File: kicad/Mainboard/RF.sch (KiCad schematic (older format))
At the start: 111 parts, among them J8 Antenna, Q3 BGA6589, Q7 FDV304P, T1 AFT05MS004NT1, U13 BGA2874, U5 ADF7021, U6 HMC546MS8GETR, U7 LM2904A, X1 12.288MHz

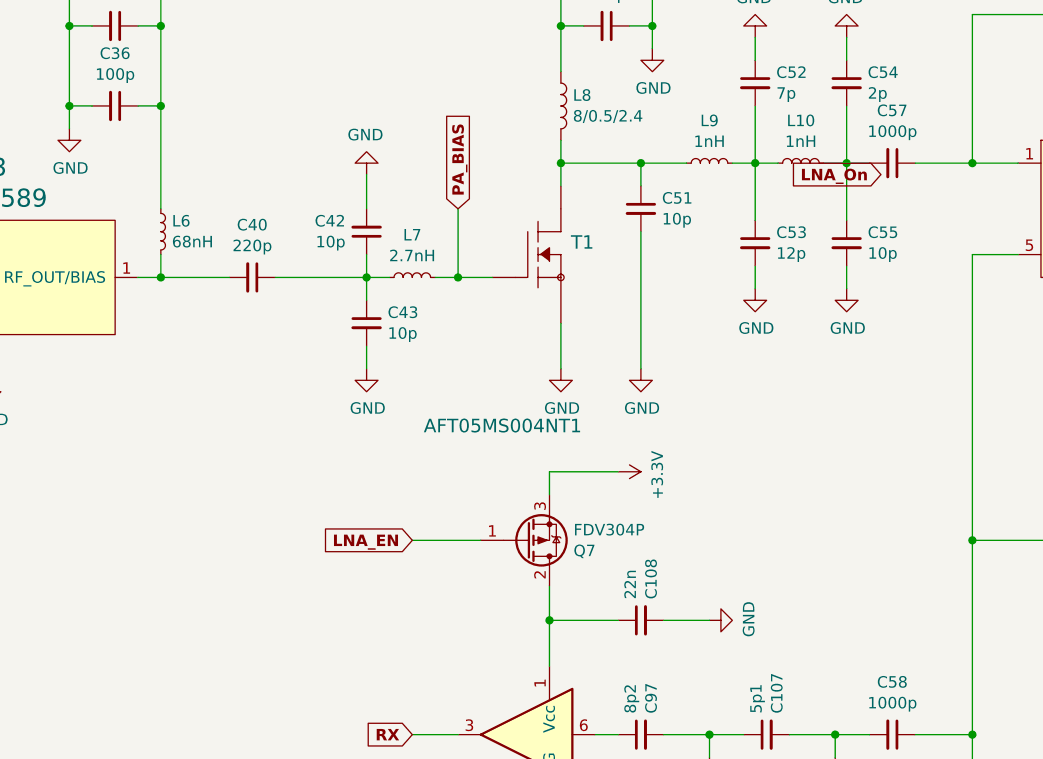
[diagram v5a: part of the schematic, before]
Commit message: Added some vias and forgotten power supply lines & plotted pdf schematic
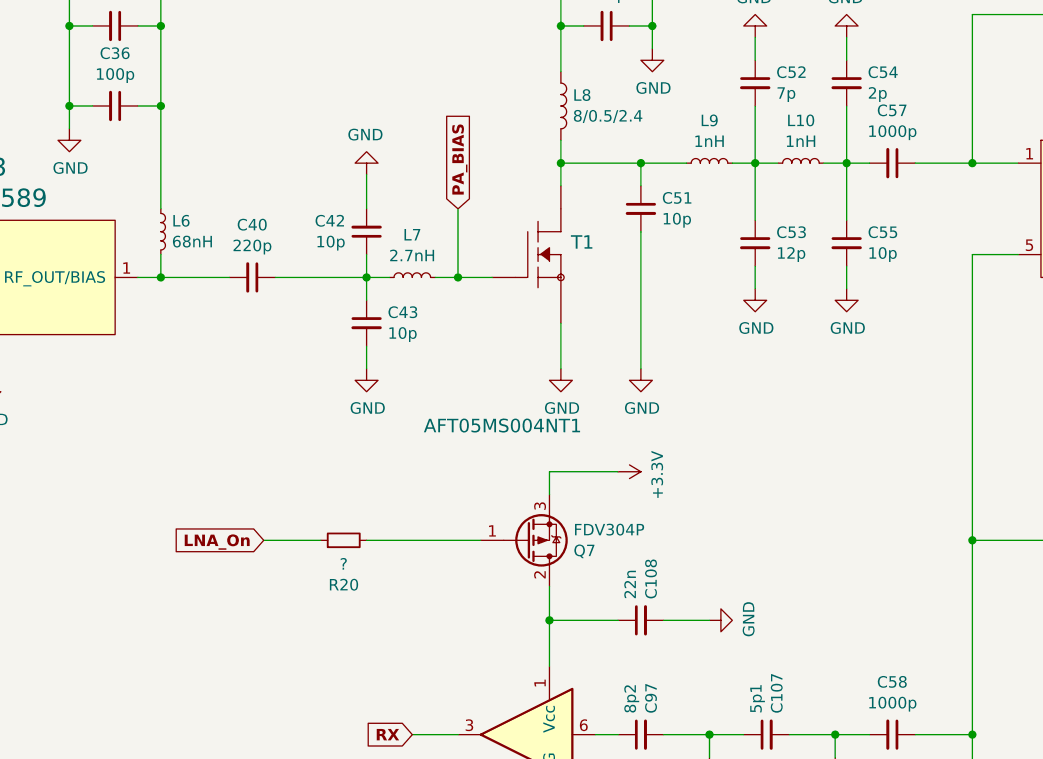
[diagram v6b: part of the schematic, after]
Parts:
- added R20: ?, Resistor_SMD:R_0603_1608Metric, symbol Mainboard-rescue:R_Small-Device
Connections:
- net LNA_On: now also R20.1
- net LNA_EN: no longer names the net of Q7.1 (G)
- net LNA_EN: now also R20.2
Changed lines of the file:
@@
 EESchema Schematic File Version 4
-LIBS:Mainboard-cache
 EELAYER 30 0
 EELAYER END
@@
 	1    0    0    1
 $EndComp
-Text GLabel 5700 4150 0    50   Input ~ 10
-LNA_EN
-Text GLabel 7750 2550 0    50   Input ~ 10
+Text GLabel 5050 4150 0    50   Input ~ 10
 LNA_On
-Wire Wire Line
-	5700 4150 6000 4150
 Wire Wire Line
 	6300 4500 6600 4500
@@
 Wire Wire Line
 	7900 5000 8150 5000
+$Comp
+L Mainboard-rescue:R_Small-Device R20
+U 1 1 5EE52FB1
+P 5400 4150
+F 0 "R20" V 5204 4150 50  0000 C CNN
+F 1 "?" V 5295 4150 50  0000 C CNN
+F 2 "Resistor_SMD:R_0603_1608Metric" H 5400 4150 50  0001 C CNN
+F 3 "~" H 5400 4150 50  0001 C CNN
+	1    5400 4150
+	0    -1   -1   0
+$EndComp
+Wire Wire Line
+	5500 4150 6000 4150
+Wire Wire Line
+	5300 4150 5050 4150
 $EndSCHEMATC

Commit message: added vias, and long soldering pads(for shielding) around RF Amplifier part, added more vias near STM32, added 3D visualizaton of PCB!
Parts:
- L8: footprint TR-9:RF_Coil -> TR-9:RF_Coil_v2_mirrored
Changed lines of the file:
@@
 F 0 "L8" H 6402 2296 50  0000 L CNN
 F 1 "8/0.5/2.4" H 6402 2205 50  0000 L CNN
-F 2 "TR-9:RF_Coil" H 6350 2250 50  0001 C CNN
+F 2 "TR-9:RF_Coil_v2_mirrored" H 6350 2250 50  0001 C CNN
 F 3 "~" H 6350 2250 50  0001 C CNN
 	1    6350 2250

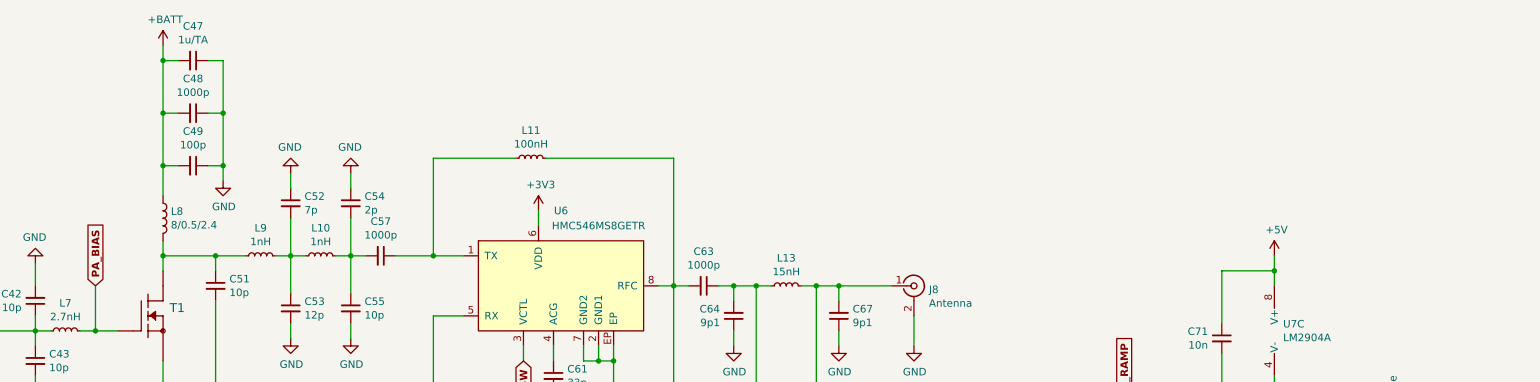
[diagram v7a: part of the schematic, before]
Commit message: added a JCx symbols - these are Jumper Cables - them are used to avoid EMI diseaster when trying to route Power signals under RF 50 ohm trace - also added them to PCB +  Schematic in PDF plotted; TODO - more signal integrity improvement
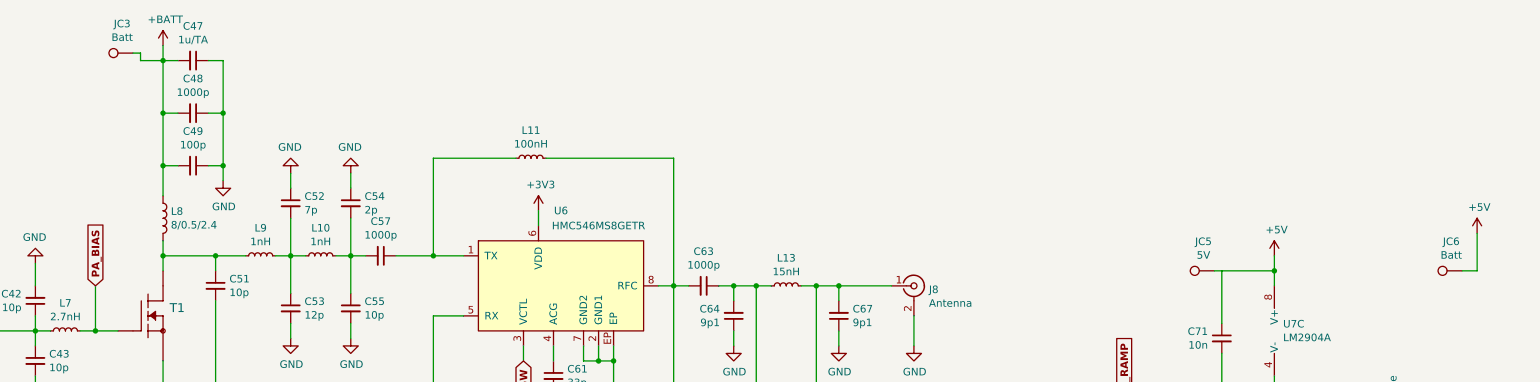
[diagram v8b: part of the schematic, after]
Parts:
- added JC3, JC6: Batt, TR-9:Pad1x3, symbol Connector:TestPoint
- added JC5: 5V, TR-9:Pad1x3, symbol Connector:TestPoint
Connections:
- net +5V: now also JC5.1, JC6.1
- net +BATT: now also JC3.1
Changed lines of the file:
@@
 Wire Wire Line
 	5300 4150 5050 4150
+$Comp
+L Connector:TestPoint JC?
+U 1 1 5F012C9B
+P 6150 1150
+AR Path="/5DFC2ACA/5F012C9B" Ref="JC?"  Part="1"
+AR Path="/5DF0E505/5F012C9B" Ref="JC3"  Part="1"
+F 0 "JC3" V 6345 1222 50  0000 C CNN
+F 1 "Batt" V 6254 1222 50  0000 C CNN
+F 2 "TR-9:Pad1x3" H 6350 1150 50  0001 C CNN
+F 3 "~" H 6350 1150 50  0001 C CNN
+	1    6150 1150
+	0    -1   -1   0
+$EndComp
+Wire Wire Line
+	6150 1150 6200 1150
+Wire Wire Line
+	6200 1150 6200 1200
+Wire Wire Line
+	6200 1200 6350 1200
+$Comp
+L Connector:TestPoint JC?
+U 1 1 5F0B8C39
+P 13350 2600
+AR Path="/5DFC2ACA/5F0B8C39" Ref="JC?"  Part="1"
+AR Path="/5DF0E505/5F0B8C39" Ref="JC5"  Part="1"
+F 0 "JC5" V 13545 2672 50  0000 C CNN
+F 1 "5V" V 13454 2672 50  0000 C CNN
+F 2 "TR-9:Pad1x3" H 13550 2600 50  0001 C CNN
+F 3 "~" H 13550 2600 50  0001 C CNN
+	1    13350 2600
+	0    -1   -1   0
+$EndComp
+Wire Wire Line
+	13350 2600 13400 2600
+$Comp
+L power:+5V #PWR0213
+U 1 1 5F0D81B0
+P 15100 2350
+F 0 "#PWR0213" H 15100 2200 50  0001 C CNN
+F 1 "+5V" H 15115 2523 50  0000 C CNN
+F 2 "" H 15100 2350 50  0001 C CNN
+F 3 "" H 15100 2350 50  0001 C CNN
+	1    15100 2350
+	1    0    0    -1
+$EndComp
+$Comp
+L Connector:TestPoint JC?
+U 1 1 5F0D8B7F
+P 15000 2600
+AR Path="/5DFC2ACA/5F0D8B7F" Ref="JC?"  Part="1"
+AR Path="/5DF0E505/5F0D8B7F" Ref="JC6"  Part="1"
+F 0 "JC6" V 15195 2672 50  0000 C CNN
+F 1 "Batt" V 15104 2672 50  0000 C CNN
+F 2 "TR-9:Pad1x3" H 15200 2600 50  0001 C CNN
+F 3 "~" H 15200 2600 50  0001 C CNN
+	1    15000 2600
+	0    -1   -1   0
+$EndComp
+Wire Wire Line
+	15100 2350 15100 2600
+Wire Wire Line
+	15000 2600 15100 2600
 $EndSCHEMATC
